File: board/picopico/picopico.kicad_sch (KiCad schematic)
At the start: 19 parts, among them J1 audio_chip, J2 display, SW3 SW_Push, SW5 SW_Push, SW6 SW_Push, SW7 SW_Push, SW8 SW_Push, U1 DollaTekESP32

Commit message: update board
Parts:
- J2: footprint Connector_PinSocket_2.54mm:PinSocket_1x08_P2.54mm_Vertical_SMD_Pin1Right -> picopico:1.77 display
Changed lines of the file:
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@@
       (effects (font (size 1.27 1.27)) (justify left))
     )
-    (property "Footprint" "Connector_PinSocket_2.54mm:PinSocket_1x08_P2.54mm_Vertical_SMD_Pin1Right" (id 2) (at 186.69 68.58 0)
+    (property "Footprint" "picopico:1.77 display" (id 2) (at 186.69 68.58 0)
       (effects (font (size 1.27 1.27)) hide)
     )
@@
   (symbol (lib_id "power:+3.3V") (at 160.02 102.87 0) (unit 1)
     (in_bom yes) (on_board yes) (fields_autoplaced)
-    (property "Reference" "#PWR?" (id 0) (at 160.02 106.68 0)
+    (property "Reference" "#PWR0101" (id 0) (at 160.02 106.68 0)
       (effects (font (size 1.27 1.27)) hide)
     )
@@
     )
     (path "/74173093-d502-4aef-8792-837fb442a2de"
-      (reference "#PWR?") (unit 1) (value "+3.3V") (footprint "")
+      (reference "#PWR0101") (unit 1) (value "+3.3V") (footprint "")
     )
     (path "/f6a4a9ed-8e48-4f7a-b558-9479f30895cb"
@@
     )
     (path "/4c6fd3c0-a295-4d12-9380-2846e41da037"
-      (reference "J2") (unit 1) (value "display") (footprint "Connector_PinSocket_2.54mm:PinSocket_1x08_P2.54mm_Vertical_SMD_Pin1Right")
+      (reference "J2") (unit 1) (value "display") (footprint "picopico:1.77 display")
     )
     (path "/b5e5f611-703a-45a2-a020-4515dd49eda4"

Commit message: update board
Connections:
- net +3V3: now also U1.1 (3v3)
- net DIN: now also U1.12 (14); no longer U1.10 (26)
- net GND: now also U1.17 (GND), U1.21 (GND), U1.34 (GND)
- net LRC: now also U1.10 (26); no longer U1.12 (14)
- net SW_B: now also R6.1, SW6.2, U1.8 (33); no longer R_SW_B1.2, SW_B1.1, U1.24 (0)
- net SW_START: now reaches R7.1, SW7.2
- net SW_START: now also U1.7 (32)
- net SW_SEL: now reaches U1.6 (35)
- net SW_SEL: now also R8.1, SW8.2
- net SW_A: now reaches U1.9 (25)
- net SW_A: now also R5.1, SW5.2
- new net SW_BOT: R_SW_B1.2, SW_B1.1, U1.24 (0)
- no-connect marks 2 -> 0
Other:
- moved on the sheet: R5, R6, R7, R8

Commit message: board stuff
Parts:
- J1: footprint Connector_PinSocket_2.54mm:PinSocket_1x07_P2.54mm_Vertical_SMD_Pin1Right -> Connector_PinHeader_2.54mm:PinHeader_1x07_P2.54mm_Vertical_SMD_Pin1Left
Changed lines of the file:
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@@
       (effects (font (size 1.27 1.27)) (justify left))
     )
-    (property "Footprint" "Connector_PinSocket_2.54mm:PinSocket_1x07_P2.54mm_Vertical_SMD_Pin1Right" (id 2) (at 60.96 81.28 0)
+    (property "Footprint" "Connector_PinHeader_2.54mm:PinHeader_1x07_P2.54mm_Vertical_SMD_Pin1Left" (id 2) (at 60.96 81.28 0)
       (effects (font (size 1.27 1.27)) hide)
     )
@@
     )
     (path "/f6a4a9ed-8e48-4f7a-b558-9479f30895cb"
-      (reference "J1") (unit 1) (value "audio_chip") (footprint "Connector_PinSocket_2.54mm:PinSocket_1x07_P2.54mm_Vertical_SMD_Pin1Right")
+      (reference "J1") (unit 1) (value "audio_chip") (footprint "Connector_PinHeader_2.54mm:PinHeader_1x07_P2.54mm_Vertical_SMD_Pin1Left")
     )
     (path "/4c6fd3c0-a295-4d12-9380-2846e41da037"

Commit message: rewire board
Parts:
- added H1, H2, H3, H4, H5: MountingHole, MountingHole:MountingHole_2.7mm_M2.5, symbol Mechanical:MountingHole
- J1: footprint Connector_PinHeader_2.54mm:PinHeader_1x07_P2.54mm_Vertical_SMD_Pin1Left -> picopico:audio
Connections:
- net BCLK: now also U1.10 (26); no longer U1.11 (27)
- net CS: now also J2.4 (Pin_4), U1.32 (22); no longer J2.7 (Pin_7), U1.27 (18)
- net DC/RS: now also J2.5 (Pin_5), U1.29 (21); no longer J2.6 (Pin_6), U1.28 (19)
- net DIN: now also U1.11 (27); no longer U1.12 (14)
- net GND: now also J2.2 (Pin_2), U1.15 (GND); no longer J1.5 (Pin_5), J2.1 (Pin_1)
- net LED/BL: now also J2.3 (Pin_3), U1.33 (23); no longer J2.8 (Pin_8), U1.26 (5)
- net LRC: now also U1.9 (25); no longer U1.10 (26)
- net RESET: now also J2.6 (Pin_6), U1.28 (19); no longer J2.5 (Pin_5), U1.29 (21)
- net SCK: now also J2.8 (Pin_8), U1.26 (5); no longer J2.3 (Pin_3), U1.33 (23)
- net SDA: now also J2.7 (Pin_7), U1.27 (18); no longer J2.4 (Pin_4), U1.32 (22)
- net SW_A: now also U1.12 (14); no longer U1.9 (25)
- net SW_B: now also U1.14 (13); no longer U1.8 (33)
- net SW_BOT: now also U1.23 (2); no longer U1.24 (0)
- net SW_SEL: now also U1.5 (34i); no longer U1.6 (35)
- net SW_START: now also U1.6 (35i); no longer U1.7 (32)
- net SW_T: now also U1.24 (0STRAP); no longer U1.23 (2)
- net +3V3 renamed +3.3V
- net +3.3V: now also J1.5 (Pin_5), J2.1 (Pin_1); no longer J2.2 (Pin_2)
- no-connect marks 0 -> 11
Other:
- moved on the sheet: J2, U1

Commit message: update board
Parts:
- added SW1: SW_SPDT, Button_Switch_THT:SW_E-Switch_EG1224_SPDT_Angled, symbol Switch:SW_SPDT
- added U2: volume_wheel, picopico:volume wheel, symbol picopico:volume_wheel
- J1: symbol Connector_Generic:Conn_01x07 -> picopico:audio
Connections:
- net VBAT: now reaches U1.16 (VBAT)
- net VBAT: now also SW1.3 (C)
- new net: J1.9 (Out_+), U2.2
- new net +BATT: SW1.2 (B)
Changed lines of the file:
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@@
   )
   (no_connect (at 154.94 93.98))
-  (no_connect (at 125.73 96.52))
+  (no_connect (at 109.22 105.41))
   (no_connect (at 154.94 96.52))
   (no_connect (at 125.73 88.9))
@@
     (stroke (width 0) (type default) (color 0 0 0 0))
   )
+  (wire (pts (xy 41.91 85.09) (xy 45.72 85.09))
+    (stroke (width 0) (type default) (color 0 0 0 0))
+  )
   (wire (pts (xy 156.21 63.5) (xy 156.21 68.58))
     (stroke (width 0) (type default) (color 0 0 0 0))
@@
     (stroke (width 0) (type default) (color 0 0 0 0))
   )
+  (wire (pts (xy 102.87 95.25) (xy 99.06 95.25))
+    (stroke (width 0) (type default) (color 0 0 0 0))
+  )
+  (wire (pts (xy 99.06 95.25) (xy 99.06 107.95))
+    (stroke (width 0) (type default) (color 0 0 0 0))
+  )
   (wire (pts (xy 80.01 139.7) (xy 85.09 139.7))
     (stroke (width 0) (type default) (color 0 0 0 0))
@@
   (label "SW_A" (at 104.14 129.54 180)
     (effects (font (size 1.27 1.27)) (justify right bottom))
+  )
+  (label "VBAT" (at 109.22 110.49 0)
+    (effects (font (size 1.27 1.27)) (justify left bottom))
   )
   (label "DC{slash}RS" (at 185.42 71.12 180)
@@
   (label "CS" (at 179.07 68.58 0)
     (effects (font (size 1.27 1.27)) (justify left bottom))
+  )
+  (label "VBAT" (at 125.73 96.52 180)
+    (effects (font (size 1.27 1.27)) (justify right bottom))
   )
   (label "RESET" (at 185.42 73.66 180)
@@
     (pin "1")
     (pin "2")
+  )
+  (symbol (lib_id "power:+BATT") (at 102.87 95.25 0) (unit 1)
+    (in_bom yes) (on_board yes) (fields_autoplaced)
+    (property "Reference" "#PWR0107" (id 0) (at 102.87 99.06 0)
+      (effects (font (size 1.27 1.27)) hide)
+    )
+    (property "Value" "+BATT" (id 1) (at 102.87 90.17 0))
+    (property "Footprint" "" (id 2) (at 102.87 95.25 0)
+      (effects (font (size 1.27 1.27)) hide)
+    )
+    (property "Datasheet" "" (id 3) (at 102.87 95.25 0)
+      (effects (font (size 1.27 1.27)) hide)
+    )
+    (pin "1")
   )
   (symbol (lib_id "Device:R") (at 57.15 149.86 90) (unit 1)
@@
     (pin "8")
   )
+  (symbol (lib_id "Switch:SW_SPDT") (at 104.14 107.95 0) (unit 1)
+    (in_bom yes) (on_board yes) (fields_autoplaced)
+    (property "Reference" "SW1" (id 0) (at 104.14 100.33 0))
+    (property "Value" "SW_SPDT" (id 1) (at 104.14 102.87 0))
+    (property "Footprint" "Button_Switch_THT:SW_E-Switch_EG1224_SPDT_Angled" (id 2) (at 104.14 107.95 0)
+      (effects (font (size 1.27 1.27)) hide)
+    )
+    (property "Datasheet" "~" (id 3) (at 104.14 107.95 0)
+      (effects (font (size 1.27 1.27)) hide)
+    )
+    (pin "1")
+    (pin "2")
+    (pin "3")
+  )
   (symbol (lib_name "+3.3V_4") (lib_id "power:+3.3V") (at 45.72 124.46 0) (unit 1)
     (in_bom yes) (on_board yes) (fields_autoplaced)
@@
     )
   )
-  (symbol (lib_id "Connector_Generic:Conn_01x07") (at 60.96 81.28 180) (unit 1)
-    (in_bom yes) (on_board yes) (fields_autoplaced)
-    (property "Reference" "J1" (id 0) (at 58.42 82.5501 0)
+  (symbol (lib_id "picopico:volume_wheel") (at 38.1 88.9 0) (unit 1)
+    (in_bom yes) (on_board yes) (fields_autoplaced)
+    (property "Reference" "U2" (id 0) (at 35.56 83.8199 0)
+      (effects (font (size 1.27 1.27)) (justify right))
+    )
+    (property "Value" "volume_wheel" (id 1) (at 35.56 86.3599 0)
+      (effects (font (size 1.27 1.27)) (justify right))
+    )
+    (property "Footprint" "picopico:volume wheel" (id 2) (at 38.1 88.9 0)
+      (effects (font (size 1.27 1.27)) hide)
+    )
+    (property "Datasheet" "" (id 3) (at 38.1 88.9 0)
+      (effects (font (size 1.27 1.27)) hide)
+    )
+    (pin "1")
+    (pin "2")
+    (pin "3")
+  )
+  (symbol (lib_id "picopico:audio") (at 60.96 82.55 180) (unit 1)
+    (in_bom yes) (on_board yes) (fields_autoplaced)
+    (property "Reference" "J1" (id 0) (at 58.42 83.8201 0)
       (effects (font (size 1.27 1.27)) (justify left))
     )
-    (property "Value" "audio_chip" (id 1) (at 58.42 80.0101 0)
+    (property "Value" "audio_chip" (id 1) (at 58.42 81.2801 0)
       (effects (font (size 1.27 1.27)) (justify left))
     )
-    (property "Footprint" "picopico:audio" (id 2) (at 60.96 81.28 0)
-      (effects (font (size 1.27 1.27)) hide)
-    )
-    (property "Datasheet" "~" (id 3) (at 60.96 81.28 0)
+    (property "Footprint" "picopico:audio" (id 2) (at 60.96 82.55 0)
+      (effects (font (size 1.27 1.27)) hide)
+    )
+    (property "Datasheet" "~" (id 3) (at 60.96 82.55 0)
       (effects (font (size 1.27 1.27)) hide)
     )
@@
     (pin "6")
     (pin "7")
+    (pin "8")
+    (pin "9")
   )
   (symbol (lib_id "Mechanical:MountingHole") (at 22.86 22.86 90) (unit 1)
@@
       (reference "#PWR0106") (unit 1) (value "+3.3V") (footprint "")
     )
+    (path "/1ac27af4-2aea-45c8-b9f6-03c927c8e9f2"
+      (reference "#PWR0107") (unit 1) (value "+BATT") (footprint "")
+    )
     (path "/fb83870a-b861-4207-a75f-cecf36d1797b"
       (reference "H1") (unit 1) (value "MountingHole") (footprint "MountingHole:MountingHole_2.7mm_M2.5")
@@
       (reference "R_SW_T1") (unit 1) (value "10K") (footprint "Resistor_SMD:R_1206_3216Metric_Pad1.30x1.75mm_HandSolder")
     )
+    (path "/602c3fd9-e40d-4357-b6c7-96ceb0dcb772"
+      (reference "SW1") (unit 1) (value "SW_SPDT") (footprint "Button_Switch_THT:SW_E-Switch_EG1224_SPDT_Angled")
+    )
     (path "/2a578eb0-d7b8-4f5e-93b5-47ece78e218c"
       (reference "SW3") (unit 1) (value "SW_Push") (footprint "Button_Switch_SMD:SW_SPST_EVQQ2")
@@
       (reference "U1") (unit 1) (value "DollaTekESP32") (footprint "picopico:DollaTecESP32")
     )
-  )
+    (path "/f2db2212-8030-49dd-9711-386cef5079fd"
+      (reference "U2") (unit 1) (value "volume_wheel") (footprint "picopico:volume wheel")
+    )
+  )

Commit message: board
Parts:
- removed H4: MountingHole, MountingHole:MountingHole_2.7mm_M2.5, symbol Mechanical:MountingHole
- removed R_SW_B1, R_SW_R1: 10K, Resistor_SMD:R_1206_3216Metric_Pad1.30x1.75mm_HandSolder, symbol Device:R
- added R3, R4: 10K, Resistor_SMD:R_1206_3216Metric_Pad1.30x1.75mm_HandSolder, symbol Device:R
- added TP1, TP2, TP3, TP4: TestPoint, TestPoint:TestPoint_Pad_1.0x1.0mm, symbol Connector:TestPoint
- renumbered R_SW_L1 to R1, R_SW_T1 to R2
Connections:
- net +3.3V: now also SW1.3 (C), U1.19 (VIN), R3.1, R4.1
- net +BATT: now also TP4.1
- net GND: now also TP3.1
- net SW_BOT: now also R3.2
- net SW_R: now also R4.2
- net at U2.1: now also TP1.1
- net at U2.3: now also TP2.1
- net VBAT: no longer names the net of U1.16 (VBAT)
- net VBAT: no longer SW1.3 (C)

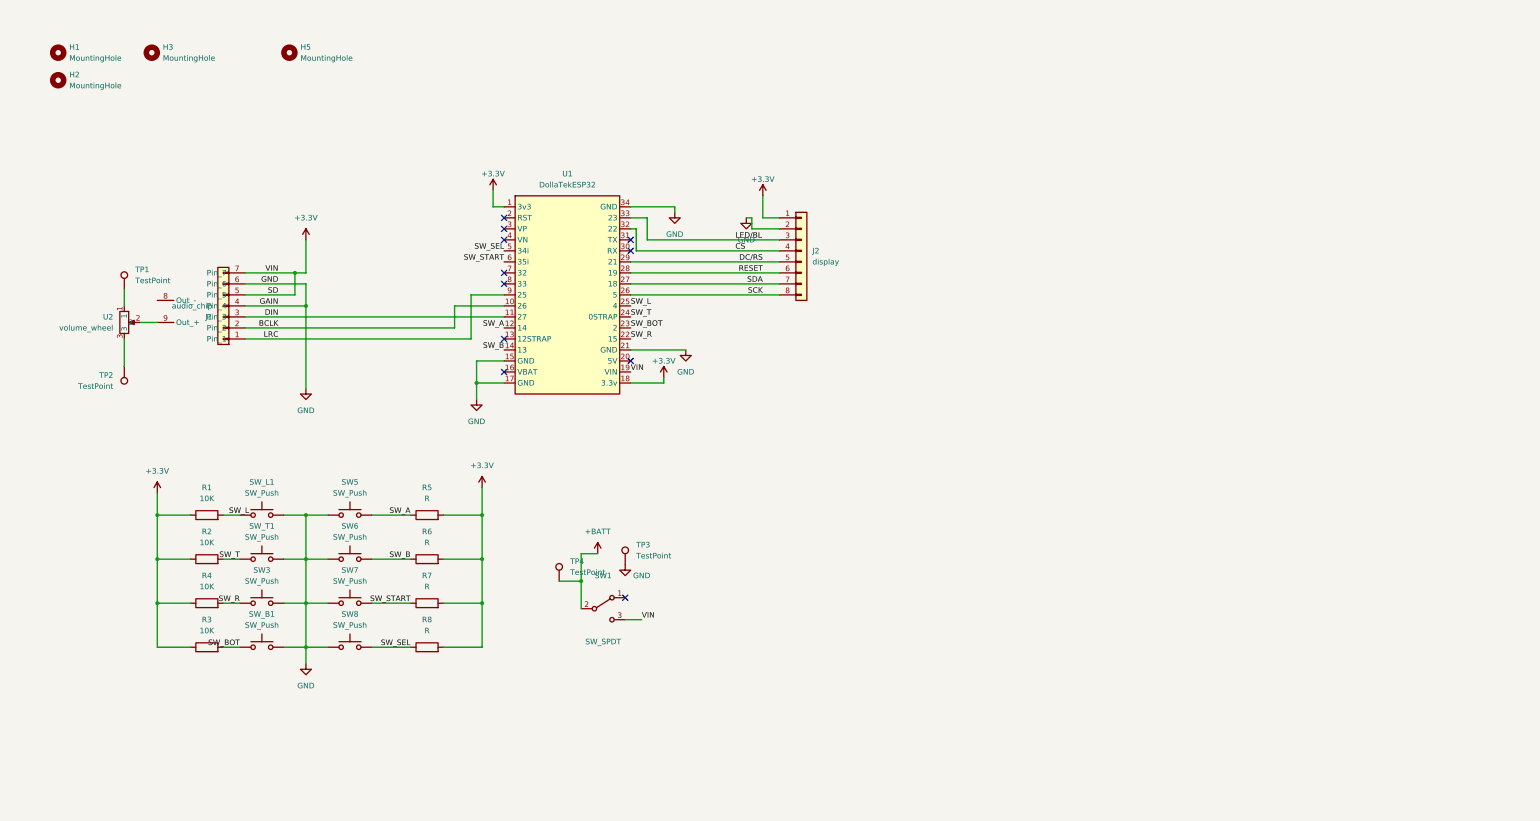
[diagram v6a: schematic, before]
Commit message: merge board v2
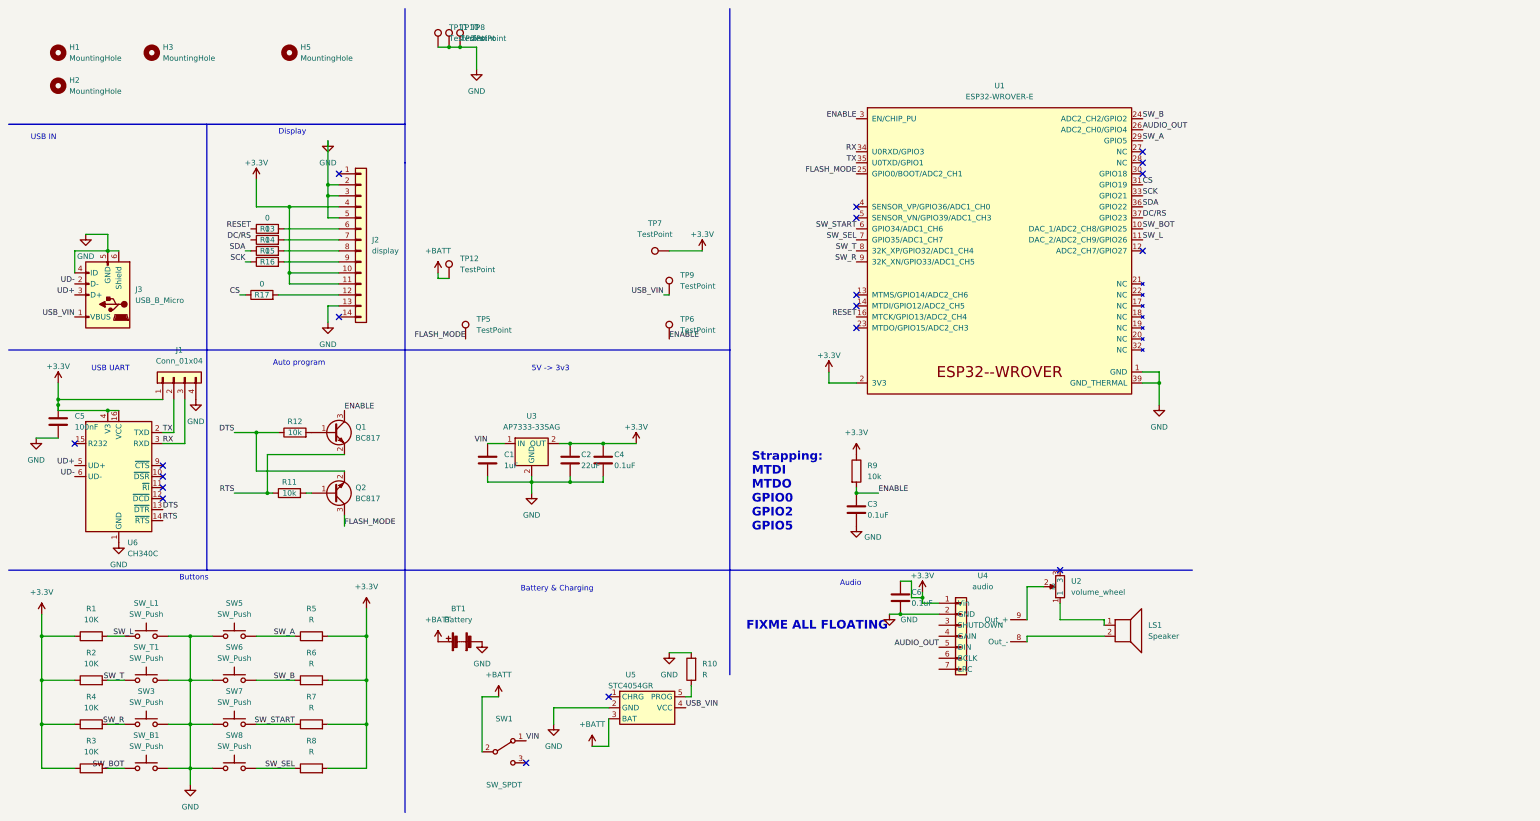
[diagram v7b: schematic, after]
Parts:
- removed J1: audio_chip, picopico:audio, symbol picopico:audio
- removed TP1, TP2, TP3, TP4: TestPoint, TestPoint:TestPoint_Pad_1.0x1.0mm, symbol Connector:TestPoint
- removed U1: DollaTekESP32, picopico:DollaTecESP32, symbol picopico:DollaTekESP32
- added BT1: Battery, picopico:SM02B-SRSS-TB, symbol Device:Battery
- added C1: 1uF, Capacitor_SMD:C_1206_3216Metric, symbol Device:C
- added C2: 22uF, Capacitor_SMD:C_1206_3216Metric, symbol Device:C
- added C3, C4, C6: 0.1uF, Capacitor_SMD:C_1206_3216Metric, symbol Device:C
- added C5: 100nF, Capacitor_SMD:C_1206_3216Metric, symbol Device:C
- added J1: Conn_01x04, Connector_PinHeader_2.54mm:PinHeader_1x04_P2.54mm_Vertical_SMD_Pin1Right, symbol Connector_Generic:Conn_01x04
- added J3: USB_B_Micro, Connector_USB:USB_Micro-B_Amphenol_10103594-0001LF_Horizontal, symbol Connector:USB_B_Micro
- added LS1: Speaker, picopico:speaker, symbol Device:Speaker
- added Q1, Q2: BC817, Package_TO_SOT_SMD:SOT-23, symbol Transistor_BJT:BC817
- added R10: R, Resistor_SMD:R_1206_3216Metric_Pad1.30x1.75mm_HandSolder, symbol Device:R
- added R11, R12, R9: 10k, Resistor_SMD:R_1206_3216Metric_Pad1.30x1.75mm_HandSolder, symbol Device:R
- added R13, R14, R15, R16, R17: 0, Resistor_SMD:R_0201_0603Metric, symbol Device:R
- added TP10, TP11, TP12, TP5, TP6, TP7, TP8, TP9: TestPoint, picopico:pad, symbol Connector:TestPoint
- added U1: ESP32-WROVER-E, Espressif:ESP32-WROVER-E_ThermalVias, symbol Espressif:ESP32-WROVER-E
- added U3: AP7333-33SAG, Package_TO_SOT_SMD:SOT-23, symbol picopico:AP7333-33SAG
- added U4: audio, picopico:audio, symbol picopico:audio
- added U5: STC4054GR, Package_TO_SOT_SMD:SOT-23-5, symbol picopico:STC4054GR
- added U6: CH340C, Package_SO:SOIC-16_3.9x9.9mm_P1.27mm, symbol Interface_USB:CH340C
- H1, H2, H3, H5: footprint MountingHole:MountingHole_2.7mm_M2.5 -> MountingHole:MountingHole_2.2mm_M2
- J2: footprint picopico:1.77 display -> picopico:lcd smd; symbol Connector_Generic:Conn_01x08 -> Connector_Generic:Conn_01x14
- SW1: footprint Button_Switch_THT:SW_E-Switch_EG1224_SPDT_Angled -> picopico:switch_slide_OS102011MA1QN1
- SW3, SW5, SW6, SW_B1, SW_L1, SW_T1: footprint Button_Switch_SMD:SW_SPST_EVQQ2 -> picopico:evqq2_compact
- SW7, SW8: footprint Button_Switch_SMD:SW_SPST_EVQQ2 -> Button_Switch_SMD:SW_SPST_B3U-1100P-B
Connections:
- net LED/BL is gone; now on net GND: J2.3 (Pin_3)
- net +3.3V: now also J2.10 (Pin_10), J2.11 (Pin_11), J2.4 (Pin_4), C2.1, C4.1, C5.1, C6.1, J1.1 (Pin_1), R9.1, TP7.1, U1.2 (3V3), U3.2 (OUT), U4.1 (Vin), U6.16 (VCC), U6.4 (V3); no longer J2.1 (Pin_1), SW1.3 (C)
- net +BATT: now also BT1.1 (+), TP12.1, U5.3 (BAT)
- net CS: now also R17.1, U1.31 (GPIO19); no longer J2.4 (Pin_4)
- net DC/RS: now also R14.1, U1.37 (GPIO23); no longer J2.5 (Pin_5)
- net GND: now also J2.13 (Pin_13), J2.5 (Pin_5), BT1.2 (-), C1.2, C2.2, C3.2, C4.2, C5.2, C6.2, J1.4 (Pin_4), J3.4 (ID), J3.5 (GND), J3.6 (Shield), R10.2, TP10.1, TP11.1, TP8.1, U1.1 (GND), U1.15 (GND), U1.38 (GND), U1.39 (GND_THERMAL), U3.2 (OUT), U4.2 (GND), U5.2 (GND), U6.1 (GND)
- net RESET: now also R13.1, U1.16 (MTCK/GPIO13/ADC2_CH4); no longer J2.6 (Pin_6)
- net SCK: now also R16.1, U1.33 (GPIO21); no longer J2.8 (Pin_8)
- net SDA: now also R15.1, U1.36 (GPIO22); no longer J2.7 (Pin_7)
- net SW_A: now also U1.29 (GPIO5)
- net SW_B: now also U1.24 (ADC2_CH2/GPIO2)
- net SW_BOT: now also U1.10 (DAC_1/ADC2_CH8/GPIO25)
- net SW_L: now also U1.11 (DAC_2/ADC2_CH9/GPIO26)
- net SW_R: now also U1.9 (32K_XN/GPIO33/ADC1_CH5)
- net SW_SEL: now also U1.7 (GPIO35/ADC1_CH7)
- net SW_START: now also U1.6 (GPIO34/ADC1_CH6)
- net SW_T: now also U1.8 (32K_XP/GPIO32/ADC1_CH4)
- net at U2.1: now also LS1.1
- net VIN: now reaches SW1.1 (A)
- net VIN: now also C1.1, U3.1 (IN)
- net at U2.2: now also U4.9 (Out_+)
- new net: J2.9 (Pin_9), R16.2
- new net: J2.6 (Pin_6), R13.2
- new net: R10.1, U5.5 (PROG)
- new net: Q2.1 (B), R11.2
- new net: Q1.1 (B), R12.2
- new net: J2.12 (Pin_12), R17.2
- new net: J2.7 (Pin_7), R14.2
- new net: J2.8 (Pin_8), R15.2
- new net: LS1.2, U4.8 (Out_-)
- new net AUDIO_OUT: U1.26 (ADC2_CH0/GPIO4), U4.5 (DIN)
- new net DTS: Q2.2 (E), R12.1, U6.13 (~{DTR})
- new net ENABLE: C3.1, Q1.3 (C), R9.2, TP6.1, U1.3 (EN/CHIP_PU)
- new net FLASH_MODE: Q2.3 (C), TP5.1, U1.25 (GPIO0/BOOT/ADC2_CH1)
- new net RTS: Q1.2 (E), R11.1, U6.14 (~{RTS})
- new net RX: J1.3 (Pin_3), U1.34 (U0RXD/GPIO3), U6.3 (RXD)
- new net TX: J1.2 (Pin_2), U1.35 (U0TXD/GPIO1), U6.2 (TXD)
- new net UD+: J3.3 (D+), U6.5 (UD+)
- new net UD-: J3.2 (D-), U6.6 (UD-)
- new net USB_VIN: J3.1 (VBUS), TP9.1, U5.4 (VCC)
- no-connect marks 11 -> 19
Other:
- note added: "5V -> 3v3"
- note added: "Audio"
- note added: "Auto program"
- note added: "Battery & Charging"
- note added: "Buttons"
- note added: "Display"
- note added: "FIXME ALL FLOATING"
- note added: "Strapping: MTDI MTDO GPIO0 GPIO2 GPIO5"
- note added: "USB IN"
- note added: "USB UART"
- moved on the sheet: H2, R1, R2, R3, R4, R5, R6, R7, R8, SW1, SW3, SW5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

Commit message: break everything to move to custom-lua
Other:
- note added: "Put SCLK on 18 MISO on 19 DS on 5 or 3v3 For hw-based SPI (on VSPI) https://docs.espressif.com/projects/esp-idf/en/latest/esp32/api-reference/peripherals/spi_master.html#gpio-matrix-and-io-mux"
- note added: "resistor on pin 4"
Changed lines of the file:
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@@
+    (effects (font (size 1.27 1.27)) (justify left bottom))
+  )
+  (text "Put\nSCLK on 18\nMISO on 19\nDS on 5 or 3v3\nFor hw-based SPI (on VSPI)\nhttps://docs.espressif.com/projects/esp-idf/en/latest/esp32/api-reference/peripherals/spi_master.html#gpio-matrix-and-io-mux"
+    (at 207.01 27.94 0)
+    (effects (font (size 1.27 1.27)) (justify left bottom))
+  )
+  (text "resistor on pin 4\n" (at 72.39 57.15 0)
     (effects (font (size 1.27 1.27)) (justify left bottom))
   )
